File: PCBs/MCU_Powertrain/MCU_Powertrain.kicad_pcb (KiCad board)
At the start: 2 copper layers, 155 parts, among them J1 PHASE_A, J2 PHASE_B, J3 PHASE_C, J4 Big Conn, J5 Pogo Conn, J6 Conn CAN, J7 PWRIN, Q1 SIZF906DT, Q2 SIZF906DT, Q3 SIZF906DT, SW1 SW_Push, SW2 SW_Push, U1 DRV8305, U2 SN65HVD232, U3 MCP2515, U4 LMR16006XDDC, U5 TMS320F28027F, U6 SN74LVC2G07, U7 SN74LVC2G07, Y1 20MHz

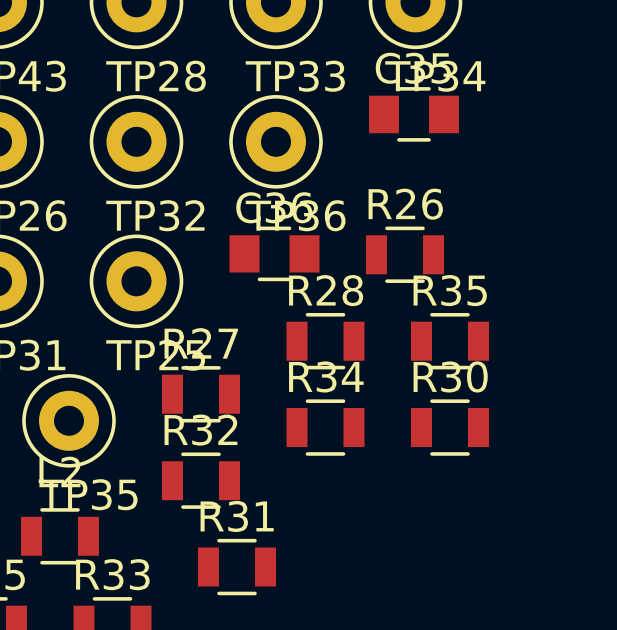
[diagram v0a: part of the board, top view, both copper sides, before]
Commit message: Small Tweaks
- Removed double CAN int pullup
- Double checked overall schematic
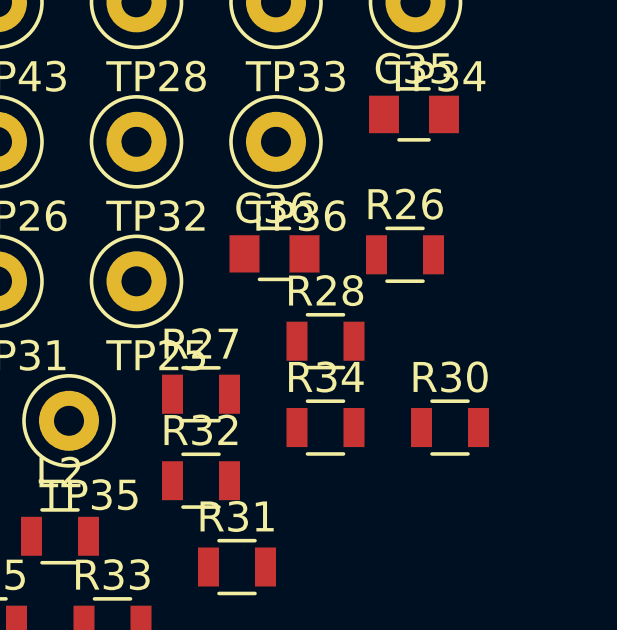
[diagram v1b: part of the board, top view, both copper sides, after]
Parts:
- removed R35: 10k, Resistors_SMD:R_0805
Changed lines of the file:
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@@
     (tracks 0)
     (zones 0)
-    (modules 155)
+    (modules 154)
     (nets 106)
   )
@@
     (solder_mask_min_width 0.25)
     (aux_axis_origin 0 0)
-    (visible_elements FFFFFF7F)
+    (visible_elements 7FFFFFFF)
     (pcbplotparams
       (layerselection 0x010fc_ffffffff)
@@
     (model ${KISYS3DMOD}/Resistors_SMD.3dshapes/R_0805.wrl
       (at (xyz 0 0 0))
-      (scale (xyz 1 1 1))
-      (rotate (xyz 0 0 0))
-    )
-  )
-  (module Resistors_SMD:R_0805 (layer F.Cu)
-    (at 132.695001 61.050001)
-    (descr "Resistor SMD 0805, reflow soldering, Vishay (see dcrcw.pdf)")
-    (tags "resistor 0805")
-    (attr smd)
-    (fp_text reference R35 (at 0 -1.65) (layer F.SilkS)
-      (effects (font (size 1 1) (thickness 0.15)))
-    )
-    (fp_text value 10k (at 0 1.75) (layer F.Fab)
-      (effects (font (size 1 1) (thickness 0.15)))
-    )
-    (fp_text user %R (at 0 0) (layer F.Fab)
-      (effects (font (size 0.5 0.5) (thickness 0.075)))
-    )
-    (fp_line (start -1 0.62) (end -1 -0.62) (layer F.Fab) (width 0.1))
-    (fp_line (start 1 0.62) (end -1 0.62) (layer F.Fab) (width 0.1))
-    (fp_line (start 1 -0.62) (end 1 0.62) (layer F.Fab) (width 0.1))
-    (fp_line (start -1 -0.62) (end 1 -0.62) (layer F.Fab) (width 0.1))
-    (fp_line (start 0.6 0.88) (end -0.6 0.88) (layer F.SilkS) (width 0.12))
-    (fp_line (start -0.6 -0.88) (end 0.6 -0.88) (layer F.SilkS) (width 0.12))
-    (fp_line (start -1.55 -0.9) (end 1.55 -0.9) (layer F.CrtYd) (width 0.05))
-    (fp_line (start -1.55 -0.9) (end -1.55 0.9) (layer F.CrtYd) (width 0.05))
-    (fp_line (start 1.55 0.9) (end 1.55 -0.9) (layer F.CrtYd) (width 0.05))
-    (fp_line (start 1.55 0.9) (end -1.55 0.9) (layer F.CrtYd) (width 0.05))
-    (pad 1 smd rect (at -0.95 0) (size 0.7 1.3) (layers F.Cu F.Paste F.Mask)
-      (net 23 +3V3))
-    (pad 2 smd rect (at 0.95 0) (size 0.7 1.3) (layers F.Cu F.Paste F.Mask)
-      (net 67 /TI_MCU/CAN_INT))
-    (model ${KISYS3DMOD}/Resistors_SMD.3dshapes/R_0805.wrl
-      (at (xyz 0 0 0))

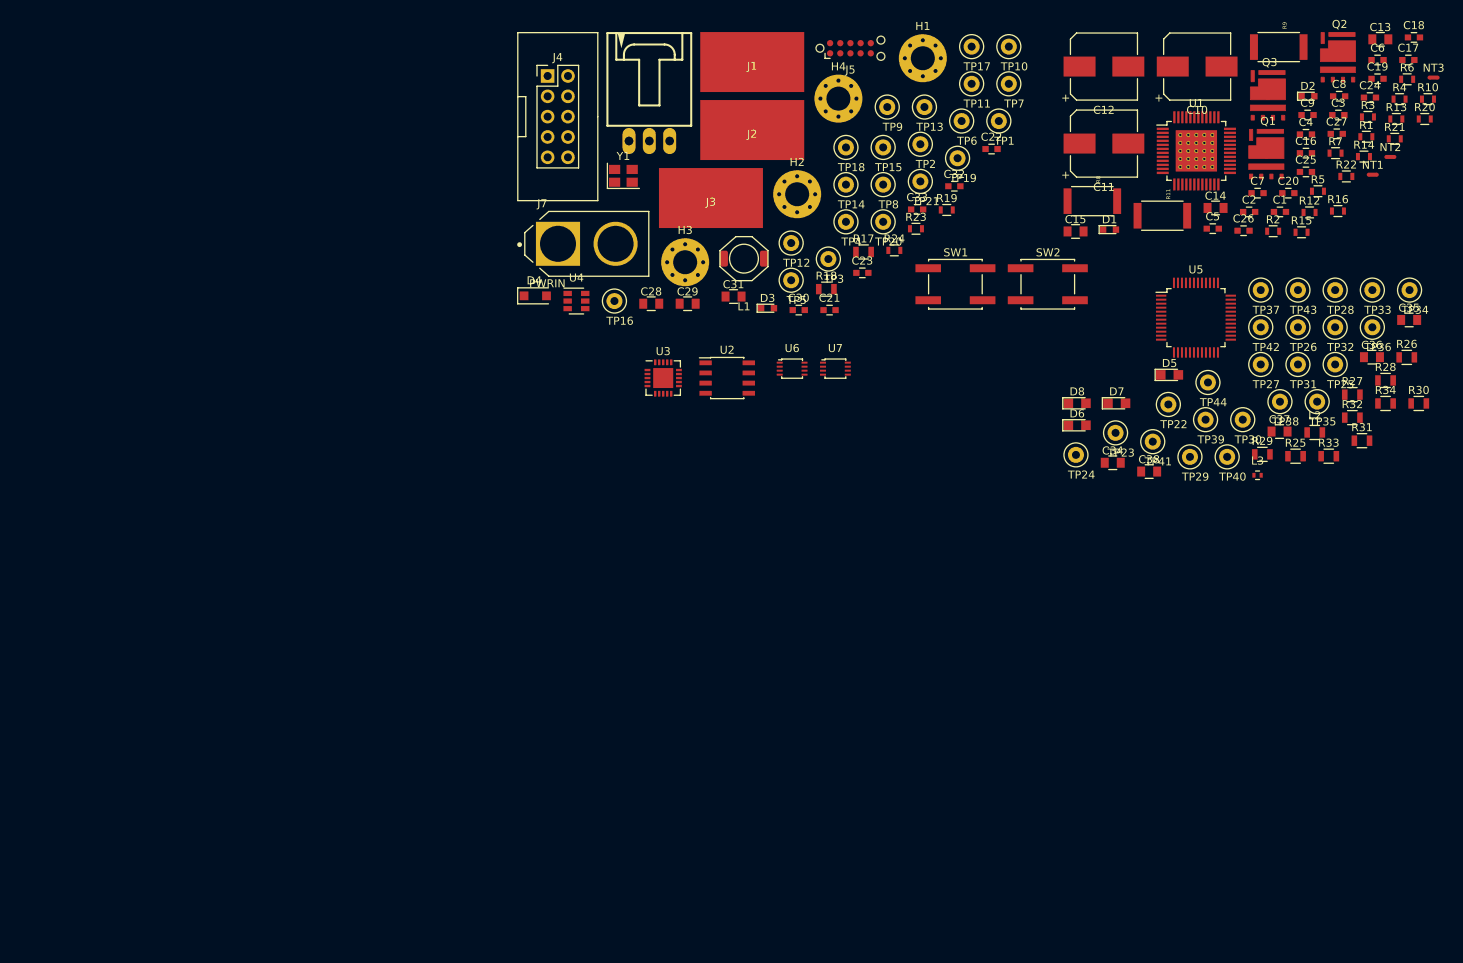
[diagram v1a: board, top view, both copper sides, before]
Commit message: Initial Layout, 3D Models, 0402s
- Changed C2, C4, C9, C16, C18 to 0402
- Some intial layout
- All 3D models added
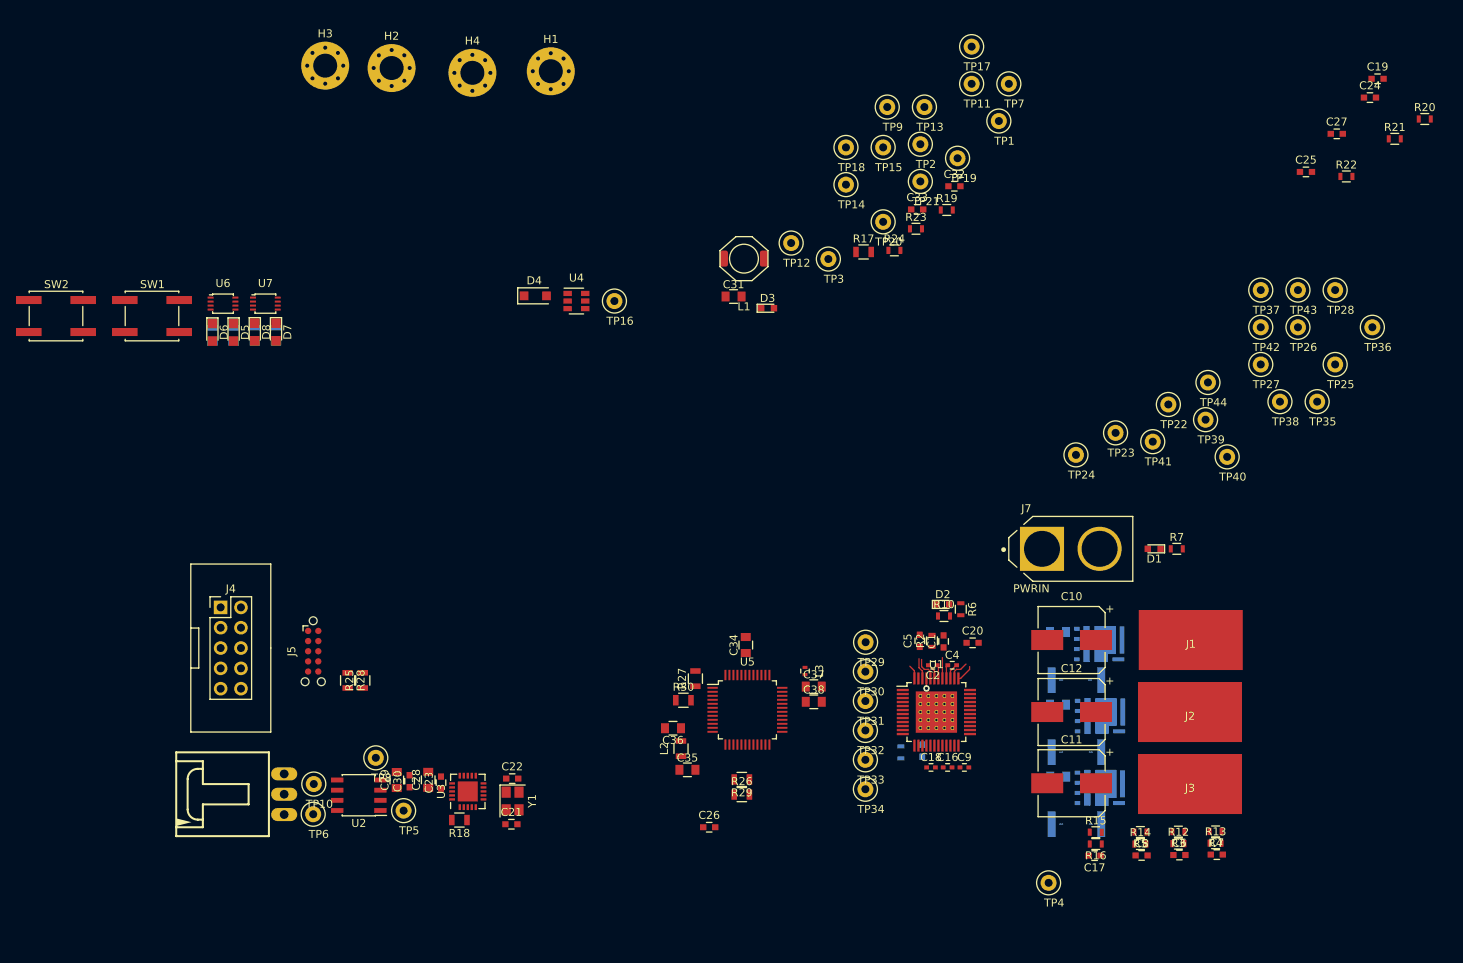
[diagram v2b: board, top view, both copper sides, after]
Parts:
- added NT4: Net-Tie_2, MCU_Powertrain:NetTie-2_SMD_5mil, B.Cu at (91.7, 107.5)
- added NT5: Net-Tie_2, MCU_Powertrain:NetTie-2_SMD_5mil, B.Cu at (91.7, 116.5)
- added NT6: Net-Tie_2, MCU_Powertrain:NetTie-2_SMD_5mil, B.Cu at (91.6, 98.5)
- C13, C14, C15, C3, Q1, Q2, Q3, R1, R11, R31, R32, R33, R34, R8, R9: moved to B.Cu
- C16, C18, C2, C4, C9: footprint Capacitors_SMD:C_0603 -> Capacitors_SMD:C_0402
- NT1, NT2, NT3: footprint NetTies:NetTie-2_SMD_Pad0.5mm -> MCU_Powertrain:NetTie-2_SMD_5mil; moved to B.Cu
- moved R32 142.9 mm to (-18.1, 55.4), turned to 270 degrees
- moved R31 141.7 mm to (-15.4, 55.4), turned to 270 degrees
- moved R34 139.0 mm to (-10.2, 55.4), turned to 270 degrees
- moved R33 135.1 mm to (-12.8, 55.4), turned to 270 degrees
- moved R28 135.1 mm to (-1.20, 98.5), turned to 270 degrees
- moved TP10 126.7 mm to (-5.42, 111.5)
- moved SW2 124.0 mm to (-37.6, 53.0)
- moved R25 119.9 mm to (0.70, 98.5), turned to 90 degrees
- moved TP6 118.7 mm to (-5.50, 115.3)
- moved D5 117.1 mm to (-15.4, 55.0), turned to 270 degrees
- moved C18 109.4 mm to (71.7, 109.4)
- moved D6 108.7 mm to (-18.1, 55.0), turned to 270 degrees
- moved C17 106.9 mm to (92.2, 120.5), turned to 180 degrees
- moved C35 106.3 mm to (41.3, 109.7)
- moved D7 105.5 mm to (-10.2, 55.0), turned to 270 degrees
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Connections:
- C16 pad 1: /Powertrain/SL_B -> /Powertrain/SN2
- C18 pad 1: /Powertrain/SL_C -> /Powertrain/SN3
- C9 pad 1: /Powertrain/SL_A -> /Powertrain/SN1
- U1 pad 19: /Powertrain/SL_C -> /Powertrain/SN3
- U1 pad 21: /Powertrain/SL_B -> /Powertrain/SN2
- U1 pad 23: /Powertrain/SL_A -> /Powertrain/SN1
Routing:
- net Net-(R2-Pad2): track 0.00 -> 3.12 mm
- net Net-(C19-Pad2): track 0.00 -> 2.71 mm
- net Net-(C5-Pad1): track 0.00 -> 2.65 mm
- net +BATT: track 0.00 -> 2.60 mm
- net Net-(C20-Pad1): track 0.00 -> 2.22 mm
- net Net-(C4-Pad2): track 0.00 -> 2.00 mm
- net Net-(C2-Pad2): track 0.00 -> 1.99 mm
- net +3V3: track 0.00 -> 1.76 mm
- net Net-(C4-Pad1): track 0.00 -> 1.72 mm
- net Net-(C2-Pad1): track 0.00 -> 1.71 mm
- net GND: track 0.00 -> 1.25 mm, vias 0 -> 1
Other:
- copper layers 2 -> 4
- rule trace_min: 0.2 -> 0.0889

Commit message: More Layout + Schematic
- Fixed small issue with net labels, ISEN labels were not seperated on the DRV sheet.
- More layout
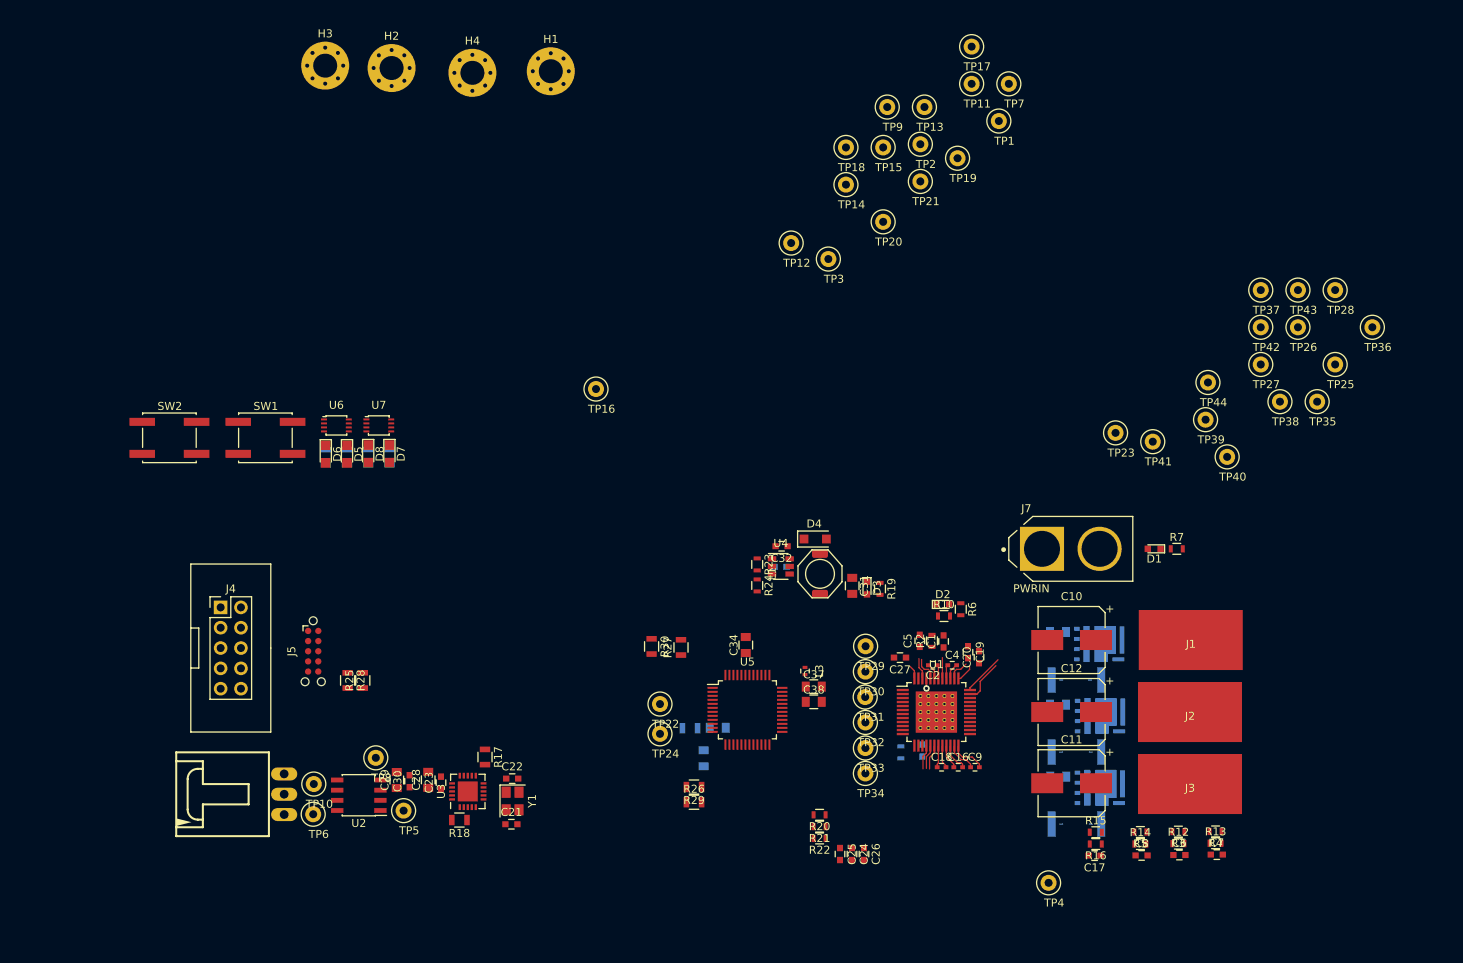
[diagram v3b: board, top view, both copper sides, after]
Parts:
- C33, C35, C36, L2: moved to B.Cu
- moved R20 115.3 mm to (57.8, 115.3), turned to 180 degrees
- moved C24 114.6 mm to (61.9, 120.2), turned to 270 degrees
- moved R21 112.1 mm to (57.8, 116.8), turned to 180 degrees
- moved R22 105.8 mm to (57.8, 118.3), turned to 180 degrees
- moved C25 103.3 mm to (60.4, 120.2), turned to 270 degrees
- moved C19 88.1 mm to (76.3, 95.0), turned to 270 degrees
- moved C27 85.3 mm to (67.8, 95.7), turned to 180 degrees
- moved R17 78.9 mm to (16.0, 108.1), turned to 270 degrees
- moved TP22 73.8 mm to (37.9, 101.5)
- moved TP24 62.6 mm to (37.9, 105.2)
- moved C32 49.9 mm to (53.0, 81.8), turned to 180 degrees
- moved R19 48.1 mm to (65.3, 87.1), turned to 270 degrees
- moved C33 47.8 mm to (52.9, 84.3), turned to 180 degrees
- moved R23 46.4 mm to (50.0, 84.0), turned to 270 degrees
- moved D4 46.4 mm to (57.2, 80.9)
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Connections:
- R20 pad 1: /TI_MCU/ADCINB1 -> /Powertrain/ISEN_A_DRV
- R21 pad 1: /TI_MCU/ADCINB3 -> /Powertrain/ISEN_B_DRV
- R22 pad 1: /TI_MCU/ADCINB7 -> /Powertrain/ISEN_C_DRV
- U1 pad 16: /TI_MCU/ADCINB1 -> /Powertrain/ISEN_A_DRV
- U1 pad 17: /TI_MCU/ADCINB3 -> /Powertrain/ISEN_B_DRV
- U1 pad 18: /TI_MCU/ADCINB7 -> /Powertrain/ISEN_C_DRV
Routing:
- net /Powertrain/SH_A: track 0.00 -> 5.41 mm
- net /Powertrain/GH_A: track 0.00 -> 5.22 mm
- net /Powertrain/SP1: track 0.00 -> 4.50 mm
- net /Powertrain/SN1: track 0.00 -> 3.88 mm
- net /Powertrain/SP2: track 0.00 -> 3.58 mm
- net /Powertrain/ISEN_C_DRV: track 0.00 -> 3.15 mm
- net /Powertrain/SN2: track 0.00 -> 3.08 mm
- net /Powertrain/ISEN_A_DRV: track 0.00 -> 3.08 mm
- net /Powertrain/ISEN_B_DRV: track 0.00 -> 3.06 mm
- net /Powertrain/SP3: track 0.00 -> 2.89 mm
- net /Powertrain/SN3: track 0.00 -> 2.76 mm

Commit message: Initial Layout
- Full initial layout complete, can probably shrink the board further as routing is complete
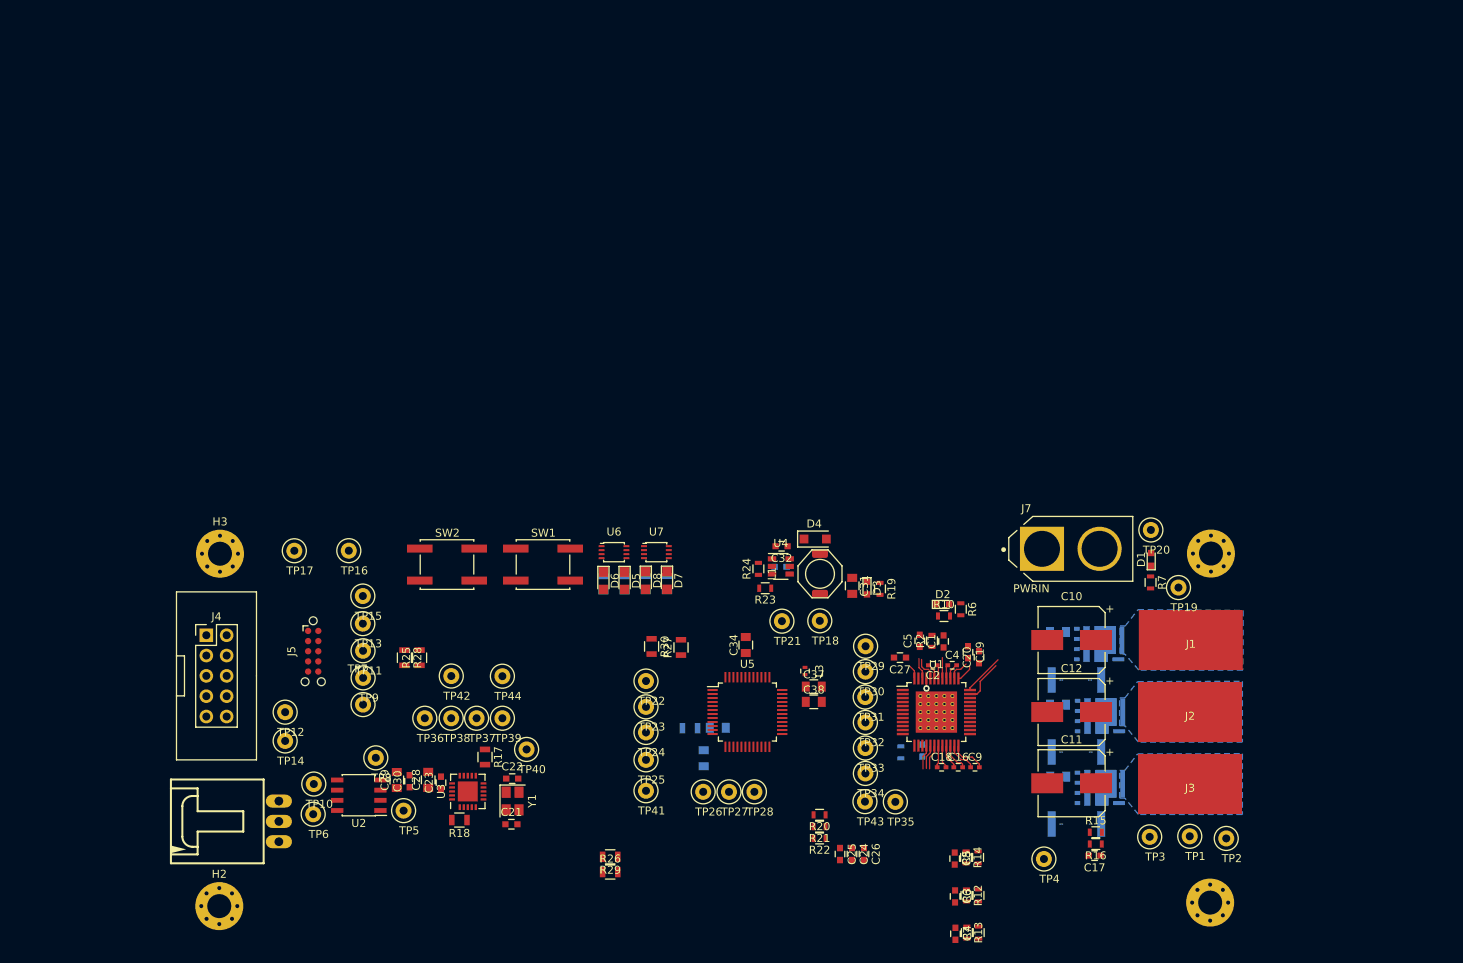
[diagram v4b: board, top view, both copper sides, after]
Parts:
- moved H1 132.6 mm to (106.6, 126.3)
- moved TP36 128.1 mm to (8.45, 103.3)
- moved TP7 112.0 mm to (0.73, 101.6)
- moved TP37 111.7 mm to (14.9, 103.3)
- moved TP38 110.9 mm to (11.8, 103.3)
- moved TP42 110.2 mm to (11.8, 98.0)
- moved H4 110.2 mm to (106.7, 82.7)
- moved H2 107.0 mm to (-17.2, 126.8)
- moved TP17 105.5 mm to (-7.86, 82.3)
- moved TP11 104.0 mm to (0.73, 94.8)
- moved TP25 99.3 mm to (36.1, 108.5)
- moved TP14 98.7 mm to (-9.01, 106.1)
- moved TP9 96.9 mm to (0.74, 98.2)
- moved TP28 95.9 mm to (49.6, 112.5)
- moved TP44 95.5 mm to (18.1, 98.0)
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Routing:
- added copper zone on B.Cu, net /Powertrain/Phase_A
- added copper zone on B.Cu, net /Powertrain/Phase_B
- added copper zone on B.Cu, net /Powertrain/Phase_C
